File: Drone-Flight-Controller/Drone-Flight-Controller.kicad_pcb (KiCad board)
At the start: 4 copper layers, 56.5 x 59.8 mm, 36 parts, among them J1 Screw_Terminal_01x02, J2 Screw_Terminal_01x03, J3 Screw_Terminal_01x03, J4 Screw_Terminal_01x03, J5 Screw_Terminal_01x03, J6 Screw_Terminal_01x02, J7 Screw_Terminal_01x03, J8 Screw_Terminal_01x04, U1 LMR51430, U2 LF33_TO220, U3 ATmega328P-P, U4 MPU-6050, U5 BMP280, Y1 16mHz

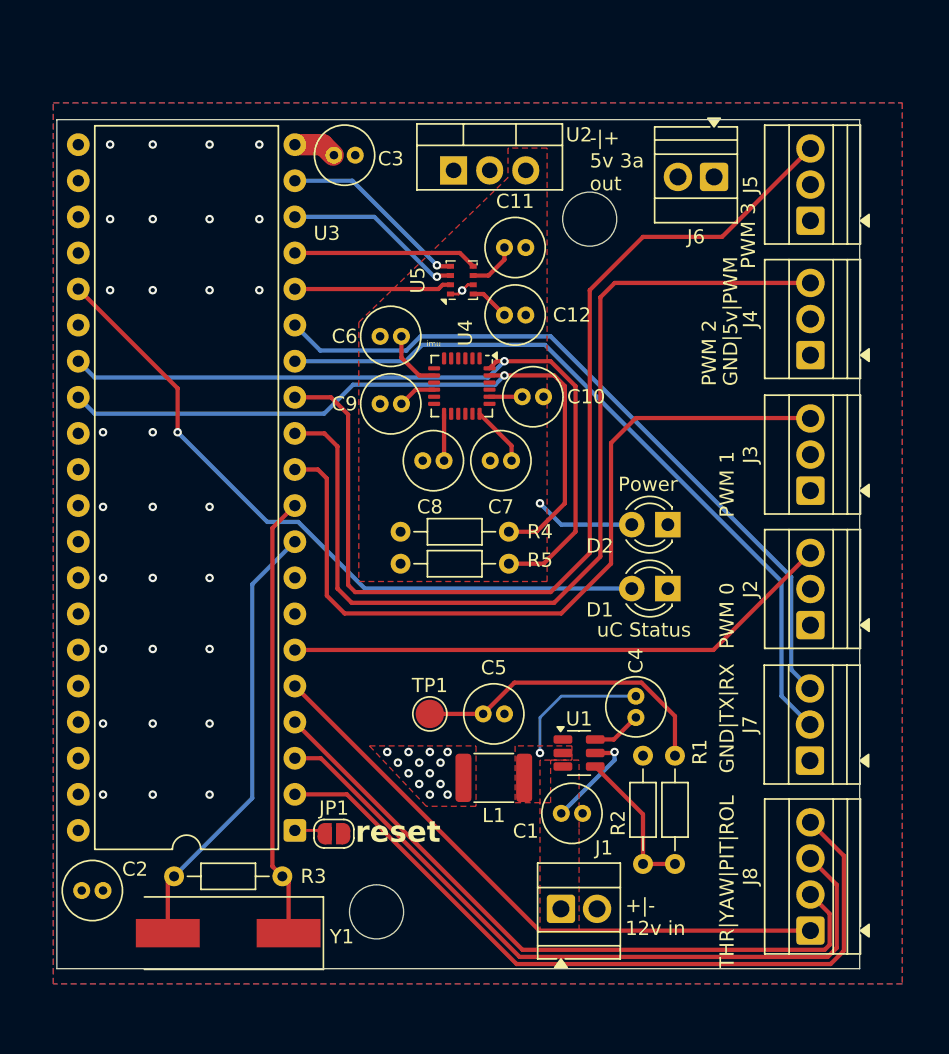
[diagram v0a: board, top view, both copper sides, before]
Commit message: move to stm32
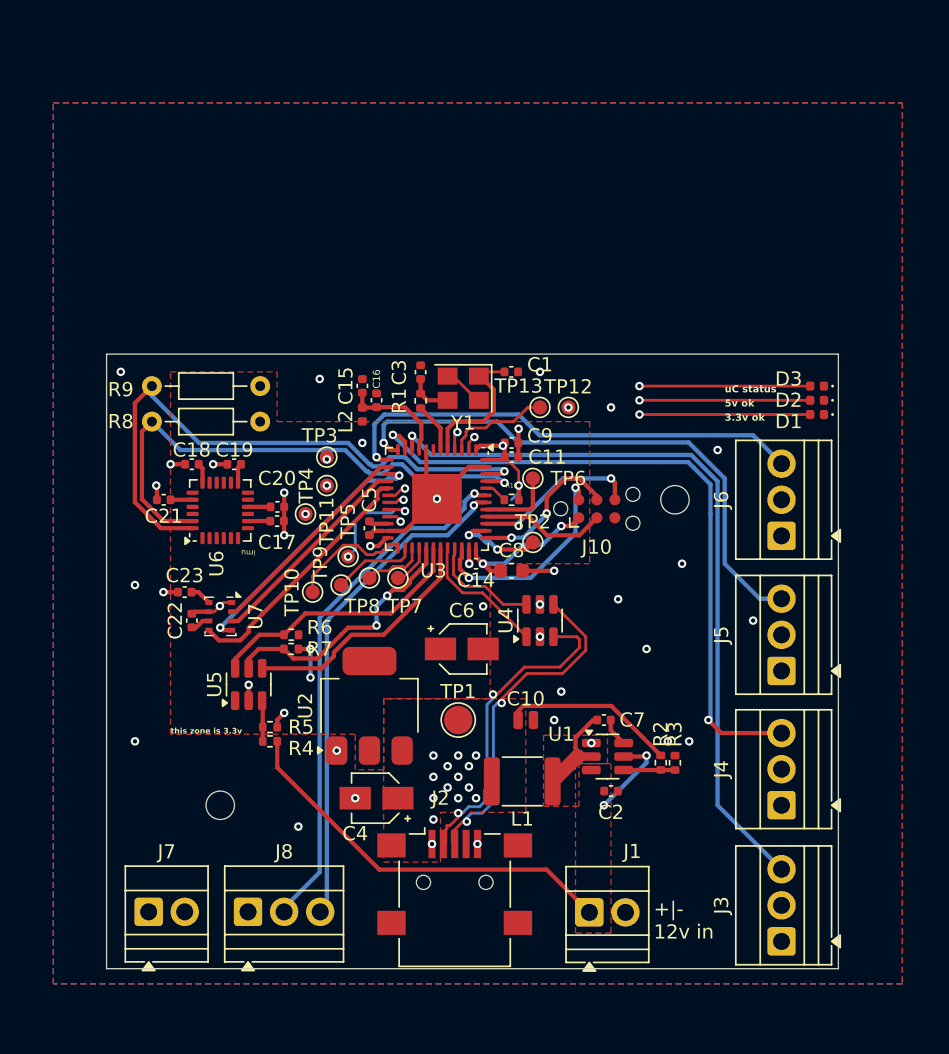
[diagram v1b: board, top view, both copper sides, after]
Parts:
- removed the C2 at (15.2, 68.5)
- removed JP1: SolderJumper_2_Open, Jumper:SolderJumper-2_P1.3mm_Open_RoundedPad1.0x1.5mm
- removed the R3 at (21.8, 67.5)
- added C1: 12p, Capacitor_SMD:C_0402_1005Metric, F.Cu at (45.5, 32.0)
- added C11: 100n, Capacitor_SMD:C_0402_1005Metric, F.Cu at (45.5, 38.0)
- added C14: 100n, Capacitor_SMD:C_0402_1005Metric, F.Cu at (43.0, 45.5)
- added C15: 1u, Capacitor_SMD:C_0402_1005Metric, F.Cu at (35.0, 33.0)
- added C16: 10n, Capacitor_SMD:C_0402_1005Metric, F.Cu at (36.0, 34.0)
- added C4: 10uF, Capacitor_SMD:CP_Elec_3x5.3, F.Cu at (36.0, 62.0)
- added C5: 2.2uF, Capacitor_SMD:C_0402_1005Metric, F.Cu at (35.5, 43.0)
- added C6: 10uF, Capacitor_SMD:CP_Elec_3x5.3, F.Cu at (42.0, 51.5)
- added C8: 4u7, Capacitor_SMD:C_0603_1608Metric, F.Cu at (45.5, 46.0)
- added C9: 100n, Capacitor_SMD:C_0402_1005Metric, F.Cu at (45.5, 37.0)
- added D3: LED, LED_SMD:LED_0402_1005Metric, F.Cu at (67.0, 33.0)
- added J10: Conn_ARM_SWD_TagConnect_TC2030-NL, Connector:Tag-Connect_TC2030-IDC-NL_2x03_P1.27mm_Vertical, F.Cu at (51.5, 41.6)
- added L2: 39n, Inductor_SMD:L_0402_1005Metric, F.Cu at (35.0, 35.0)
- added R1: 47, Resistor_SMD:R_0402_1005Metric, F.Cu at (39.1, 34.0)
- added R10: 10k, Resistor_SMD:R_0402_1005Metric, F.Cu at (45.5, 41.0)
- added R4: 1.5kOhm, Resistor_SMD:R_0402_1005Metric, F.Cu at (28.5, 58.0)
- added R5: 1kOhm, Resistor_SMD:R_0402_1005Metric, F.Cu at (28.5, 57.0)
- added R6: 10kOhm, Resistor_SMD:R_0402_1005Metric, F.Cu at (30.0, 50.5)
- added R7: 10kOhm, Resistor_SMD:R_0402_1005Metric, F.Cu at (30.0, 51.5)
- added TP10: TestPoint, TestPoint:TestPoint_Pad_D1.0mm, F.Cu at (31.5, 47.5)
- added TP11: TestPoint, TestPoint:TestPoint_Pad_D1.0mm, F.Cu at (31.0, 42.0)
- added TP12: TestPoint, TestPoint:TestPoint_Pad_D1.0mm, F.Cu at (49.5, 34.5)
- added TP13: TestPoint, TestPoint:TestPoint_Pad_D1.0mm, F.Cu at (47.5, 34.5)
- added TP2: TestPoint, TestPoint:TestPoint_Pad_D1.0mm, F.Cu at (47.0, 44.0)
- added TP3: TestPoint, TestPoint:TestPoint_Pad_D1.0mm, F.Cu at (32.5, 38.0)
- added TP4: TestPoint, TestPoint:TestPoint_Pad_D1.0mm, F.Cu at (32.5, 40.0)
- added TP5: TestPoint, TestPoint:TestPoint_Pad_D1.0mm, F.Cu at (34.0, 45.0)
- added TP6: TestPoint, TestPoint:TestPoint_Pad_D1.0mm, F.Cu at (47.0, 39.5)
- added TP7: TestPoint, TestPoint:TestPoint_Pad_D1.0mm, F.Cu at (37.5, 46.5)
- added TP8: TestPoint, TestPoint:TestPoint_Pad_D1.0mm, F.Cu at (35.5, 46.5)
- added TP9: TestPoint, TestPoint:TestPoint_Pad_D1.0mm, F.Cu at (33.5, 47.0)
- added U4: USBLC6-2SC6, Package_TO_SOT_SMD:SOT-23-6, F.Cu at (47.5, 49.5)
- added U5: ADC101C021CIMK, Package_TO_SOT_SMD:SOT-23-6, F.Cu at (27.0, 54.0)
- C10: renamed from C5; footprint Capacitor_THT:C_Radial_D4.0mm_H5.0mm_P1.50mm -> Capacitor_SMD:C_0504_1310Metric
- C17: renamed from C6; footprint Capacitor_THT:C_Radial_D4.0mm_H5.0mm_P1.50mm -> Capacitor_SMD:C_0402_1005Metric
- C18: renamed from C7; footprint Capacitor_THT:C_Radial_D4.0mm_H5.0mm_P1.50mm -> Capacitor_SMD:C_0402_1005Metric
- C19: renamed from C8; footprint Capacitor_THT:C_Radial_D4.0mm_H5.0mm_P1.50mm -> Capacitor_SMD:C_0402_1005Metric
- C2: renamed from C1; footprint Capacitor_THT:C_Radial_D4.0mm_H5.0mm_P1.50mm -> Capacitor_SMD:C_0402_1005Metric
- C20: renamed from C9; footprint Capacitor_THT:C_Radial_D4.0mm_H5.0mm_P1.50mm -> Capacitor_SMD:C_0402_1005Metric
- C21: renamed from C10; footprint Capacitor_THT:C_Radial_D4.0mm_H5.0mm_P1.50mm -> Capacitor_SMD:C_0402_1005Metric
- C22: renamed from C11; footprint Capacitor_THT:C_Radial_D4.0mm_H5.0mm_P1.50mm -> Capacitor_SMD:C_0402_1005Metric
- C23: renamed from C12; footprint Capacitor_THT:C_Radial_D4.0mm_H5.0mm_P1.50mm -> Capacitor_SMD:C_0402_1005Metric
- C3: value 100nF -> 12p; footprint Capacitor_THT:C_Radial_D4.0mm_H5.0mm_P1.50mm -> Capacitor_SMD:C_0402_1005Metric
- C7: renamed from C4; footprint Capacitor_THT:C_Radial_D4.0mm_H5.0mm_P1.50mm -> Capacitor_SMD:C_0402_1005Metric
- D1, D2: footprint LED_THT:LED_D3.0mm -> LED_SMD:LED_0402_1005Metric
- J2: value Screw_Terminal_01x03 -> USB_B_Micro; footprint TerminalBlock:TerminalBlock_Xinya_XY308-2.54-3P_1x03_P2.54mm_Horizontal -> Connector_USB:USB_Mini-B_Lumberg_2486_01_Horizontal
- J6: value Screw_Terminal_01x02 -> Screw_Terminal_01x03; footprint TerminalBlock:TerminalBlock_Xinya_XY308-2.54-2P_1x02_P2.54mm_Horizontal -> TerminalBlock:TerminalBlock_Xinya_XY308-2.54-3P_1x03_P2.54mm_Horizontal
- J7: value Screw_Terminal_01x03 -> Screw_Terminal_01x02; footprint TerminalBlock:TerminalBlock_Xinya_XY308-2.54-3P_1x03_P2.54mm_Horizontal -> TerminalBlock:TerminalBlock_Xinya_XY308-2.54-2P_1x02_P2.54mm_Horizontal
- J8: value Screw_Terminal_01x04 -> Screw_Terminal_01x03; footprint TerminalBlock:TerminalBlock_Xinya_XY308-2.54-4P_1x04_P2.54mm_Horizontal -> TerminalBlock:TerminalBlock_Xinya_XY308-2.54-3P_1x03_P2.54mm_Horizontal
- R2: renamed from R1; footprint Resistor_THT:R_Axial_DIN0204_L3.6mm_D1.6mm_P7.62mm_Horizontal -> Resistor_SMD:R_0402_1005Metric
- R3: renamed from R2; footprint Resistor_THT:R_Axial_DIN0204_L3.6mm_D1.6mm_P7.62mm_Horizontal -> Resistor_SMD:R_0402_1005Metric
- U2: value LF33_TO220 -> NCP1117-3.3_SOT223; footprint Package_TO_SOT_THT:TO-220-3_Vertical -> Package_TO_SOT_SMD:SOT-223-3_TabPin2
- U3: value ATmega328P-P -> STM32F401CBUx; footprint Package_DIP:DIP-40_W15.24mm -> Package_DFN_QFN:QFN-48-1EP_7x7mm_P0.5mm_EP3.5x3.5mm
- Y1: value 16mHz -> 16MHz; footprint Crystal:Crystal_SMD_HC49-SD -> Crystal:Crystal_SMD_3225-4Pin_3.2x2.5mm
- moved J7 47.7 mm to (20.0, 70.0), turned to 0 degrees
- moved Y1 41.8 mm to (42.1, 33.1)
- moved J8 39.6 mm to (27.0, 70.0), turned to 0 degrees
- moved U2 38.1 mm to (35.5, 55.5), turned to 90 degrees
- moved C22 34.2 mm to (23.0, 49.5), turned to 90 degrees
- moved J3 31.8 mm to (64.5, 72.1)
- moved J5 31.8 mm to (64.5, 53.0)
- moved J4 31.7 mm to (64.5, 62.5)
- moved C23 30.9 mm to (22.5, 47.5), turned to 0 degrees
- moved J2 30.9 mm to (41.5, 67.9), turned to 0 degrees
- moved U7 29.1 mm to (25.0, 49.2), turned to -90 degrees
- moved C21 26.3 mm to (21.0, 41.0), turned to 180 degrees
- moved J6 25.7 mm to (64.5, 43.5), turned to 90 degrees
- moved U3 25.4 mm to (40.2, 40.9), turned to -90 degrees
- moved C18 22.5 mm to (23.0, 38.5)
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- renumbered R4 to R8, R5 to R9, U4 to U6, U5 to U7
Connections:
- C3 pad 1: +5V -> Net-(C3-Pad1)
- D1 pad 2: Net-(D1-A) -> +3.3V
- D2 pad 2: +3.3V -> +5V
- J2 pad 1: GND -> +5V
- J2 pad 2: +5V -> USB_CONN_D-
- J2 pad 3: PWM_0 -> USB_CONN_D+
- J3 pad 3: PWM_1 -> PWM_0
- J4 pad 3: PWM_2 -> PWM_1
- J5 pad 3: PWM_3 -> PWM_2
- J6 pad 1: +5V -> GND
- J6 pad 2: GND -> +5V
- J7 pad 1: GND -> +5V
- J7 pad 2: UART_TX -> GND
- J8 pad 1: CONTROLLER_THROTTLE -> GND
- J8 pad 2: CONTROLLER_YAW -> UART_RX
- J8 pad 3: CONTROLLER_PITCH -> UART_TX
- U2 pad 1: +5V -> GND
- U2 pad 2: GND -> +3.3V
- U2 pad 3: +3.3V -> +5V
- U3 pad 1: Net-(JP1-A) -> +3.3V
- U3 pad 10: Net-(U3-XTAL2/PB7) -> PWM_0
- U3 pad 14: UART_TX -> BAROMETER_CSB
- U3 pad 15: UART_RX -> BAROMETER_SCK
- U3 pad 16: BAROMETER_CSB -> BAROMETER_SDI
- U3 pad 18: BAROMETER_SDI -> Net-(U3-PB0)
- U3 pad 19: BAROMETER_SCK -> Net-(U3-PB1)
- U3 pad 2: CONTROLLER_ROLL -> Net-(U3-PC13)
- U3 pad 20: +5V -> Net-(U3-PB2)
- U3 pad 22: GND -> Net-(U3-VCAP1)
- U3 pad 23: unconnected-(U3-PC0-Pad23) -> GND
- U3 pad 24: unconnected-(U3-PC1-Pad24) -> +3.3V
- U3 pad 25: Net-(D1-A) -> Net-(U3-PB12)
- U3 pad 26: unconnected-(U3-PC3-Pad26) -> Net-(U3-PB13)
- U3 pad 27: IMU_SDA -> Net-(U3-PB14)
- U3 pad 28: IMU_SCL -> Net-(U3-PB15)
- U3 pad 29: (no net) -> BATVOLTAGE_SCL
- U3 pad 3: CONTROLLER_PITCH -> Net-(U3-PC14)
- U3 pad 30: (no net) -> BATVOLTAGE_SDA
- U3 pad 31: (no net) -> BATVOLTAGE_ADDR
- U3 pad 32: (no net) -> USB_D-
- U3 pad 33: (no net) -> USB_D+
- U3 pad 34: (no net) -> SWDIO
- U3 pad 35: (no net) -> GND
- U3 pad 36: (no net) -> +3.3V
- U3 pad 37: (no net) -> SWCLK
- U3 pad 38: (no net) -> Net-(U3-PA15)
- U3 pad 39: (no net) -> SWO
- U3 pad 4: CONTROLLER_YAW -> LED_STATUS
- U3 pad 40: (no net) -> JTRST
- U3 pad 5: CONTROLLER_THROTTLE -> Net-(U3-PH0)
- U3 pad 6: PWM_0 -> Net-(U3-PH1)
- U3 pad 7: +5V -> NRST
- U3 pad 9: Net-(U3-XTAL1/PB6) -> +3.3VA
- U6 pad 9: unconnected-(U4-AD0-Pad9) -> IMU_ADDR
- Y1 pad 1: Net-(U3-XTAL2/PB7) -> Net-(U3-PH0)
- Y1 pad 2: Net-(U3-XTAL1/PB6) -> GND
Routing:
- net +3.3V: track 21.0 -> 80.5 mm, vias 1 -> 10
- net CONTROLLER_ROLL: track 54.0 -> 0.00 mm
- net CONTROLLER_PITCH: track 51.3 -> 0.00 mm
- net Net-(D1-A): track 49.5 -> 0.00 mm, vias 1 -> 0
- net CONTROLLER_YAW: track 48.5 -> 0.00 mm
- net CONTROLLER_THROTTLE: track 43.4 -> 0.00 mm
- net Net-(U3-PB10): track 53.5 -> 10.4 mm, vias 0 -> 2
- net PWM_3: track 72.8 -> 33.6 mm, vias 0 -> 1
- net GND: track 1.87 -> 34.4 mm, vias 30 -> 34
- net Net-(U3-XTAL1/PB6): track 31.3 -> 0.00 mm
- net Net-(U3-XTAL2/PB7): track 31.2 -> 0.00 mm
- net PWM_2: track 67.1 -> 39.2 mm, vias 0 -> 1
- net LED_STATUS: track 0.00 -> 27.5 mm, vias 0 -> 2
- net +12V: track 7.26 -> 34.4 mm, vias 1 -> 2
- net USB_CONN_D+: track 0.00 -> 24.0 mm, vias 0 -> 2
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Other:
- board size 56.5 x 59.8 mm -> 51.5 x 43.2 mm
- board text added: "3.3v ok"
- board text added: "5v ok"
- board text added: "this zone is 3.3v"
- board text added: "uC status"
- board text removed: "-|+ 5v 3a out"
- board text removed: "GND|5v|PWM"
- board text removed: "GND|TX|RX"
- board text removed: "PWM 0"
- board text removed: "PWM 1"
- board text removed: "PWM 2"
- board text removed: "PWM 3"
- board text removed: "Power"
- board text removed: "THR|YAW|PIT|ROL"
- board text removed: "reset"
- board text removed: "uC Status"

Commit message: move to more powerful mcu
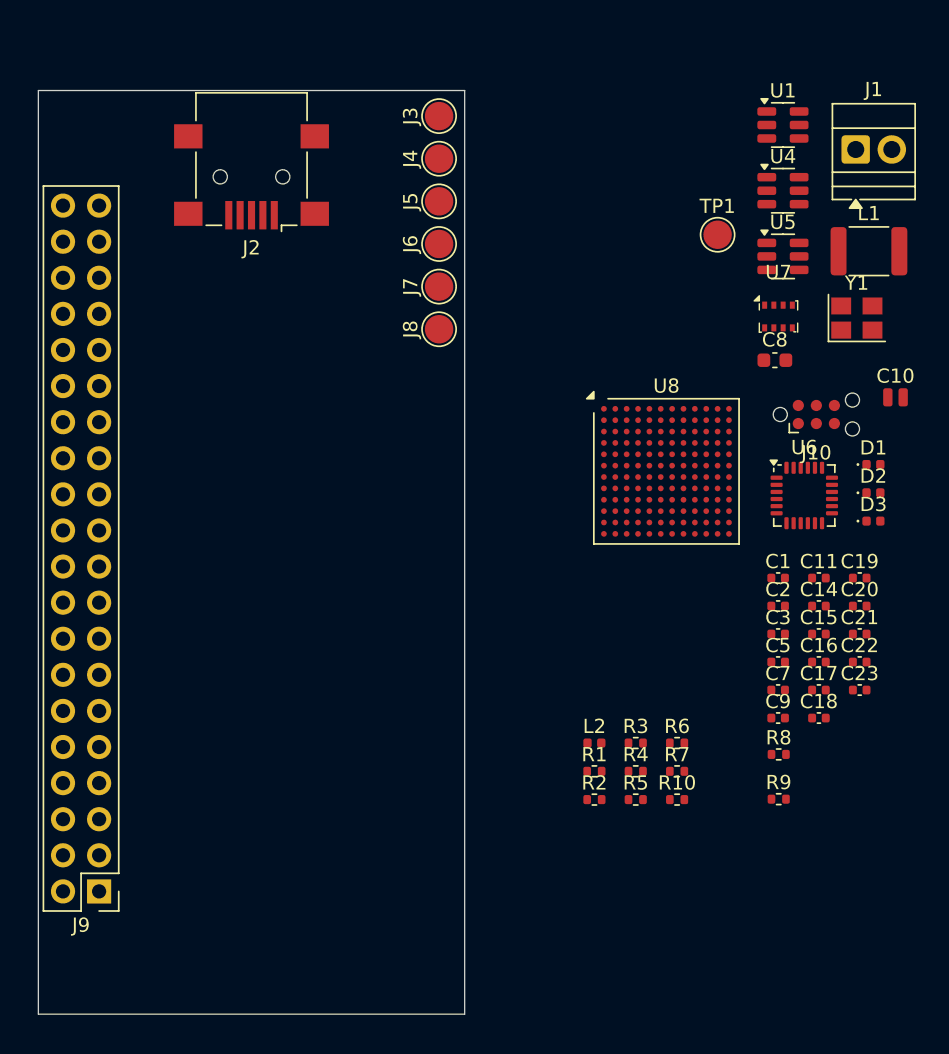
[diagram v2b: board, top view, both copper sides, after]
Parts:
- removed C4, C6: 10uF, Capacitor_SMD:CP_Elec_3x5.3
- removed TP10, TP11, TP12, TP13, TP2, TP3, TP4, TP5, TP6, TP7, TP8, TP9: TestPoint, TestPoint:TestPoint_Pad_D1.0mm
- removed U2: NCP1117-3.3_SOT223, Package_TO_SOT_SMD:SOT-223-3_TabPin2
- removed U3: STM32F401CBUx, Package_DFN_QFN:QFN-48-1EP_7x7mm_P0.5mm_EP3.5x3.5mm
- added J9: Raspberry_Pi_4, Connector_PinHeader_2.54mm:PinHeader_2x20_P2.54mm_Vertical, F.Cu at (16.5, 68.6)
- added U8: STM32F413ZHJx, Package_BGA:UFBGA-144_10x10mm_Layout12x12_P0.8mm, F.Cu at (56.4, 39.0)
- J3, J4, J5, J6, J8: value Screw_Terminal_01x03 -> TestPoint; footprint TerminalBlock:TerminalBlock_Xinya_XY308-2.54-3P_1x03_P2.54mm_Horizontal -> TestPoint:TestPoint_Pad_D2.0mm
- J7: value Screw_Terminal_01x02 -> TestPoint; footprint TerminalBlock:TerminalBlock_Xinya_XY308-2.54-2P_1x02_P2.54mm_Horizontal -> TestPoint:TestPoint_Pad_D2.0mm
- R8, R9: footprint Resistor_THT:R_Axial_DIN0204_L3.6mm_D1.6mm_P7.62mm_Horizontal -> Resistor_SMD:R_0402_1005Metric
- moved J3 62.9 mm to (40.4, 14.0)
- moved J1 56.9 mm to (69.7, 16.4)
- moved J2 51.7 mm to (27.2, 18.3), turned to 180 degrees
- moved J4 51.5 mm to (40.4, 17.0)
- moved C21 49.9 mm to (70.0, 50.5), turned to 0 degrees
- moved J7 48.5 mm to (40.4, 26.0), turned to 90 degrees
- moved U5 48.2 mm to (64.6, 23.9), turned to 0 degrees
- moved C23 48.0 mm to (70.0, 54.4)
- moved C18 47.6 mm to (67.1, 56.4), turned to 0 degrees
- moved C22 47.1 mm to (70.0, 52.4), turned to 0 degrees
- moved R9 46.7 mm to (64.3, 62.1), turned to 0 degrees
- moved U1 46.1 mm to (64.6, 14.6)
- moved C19 44.7 mm to (70.0, 46.5)
- moved U7 44.6 mm to (64.3, 28.1), turned to 0 degrees
- moved L1 44.6 mm to (70.7, 23.5), turned to 0 degrees
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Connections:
- C5 pad 2: Net-(U3-VCAP1) -> unconnected-(C5-Pad2)
- J3 pad 1: GND -> PWM_0
- J4 pad 1: GND -> PWM_1
- J5 pad 1: GND -> PWM_2
- J6 pad 1: GND -> PWM_3
- R1 pad 1: Net-(U3-PH1) -> unconnected-(R1-Pad1)
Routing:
- net +3.3V: track 80.5 -> 0.00 mm, vias 10 -> 0
- net PWM_0: track 53.0 -> 0.00 mm, vias 1 -> 0
- net PWM_1: track 47.6 -> 0.00 mm, vias 2 -> 0
- net IMU_SDA: track 43.1 -> 0.00 mm, vias 1 -> 0
- net PWM_2: track 39.2 -> 0.00 mm, vias 1 -> 0
- net IMU_SCL: track 38.5 -> 0.00 mm, vias 1 -> 0
- net UART_RX: track 37.2 -> 0.00 mm, vias 1 -> 0
- net UART_TX: track 35.2 -> 0.00 mm, vias 1 -> 0
- net +12V: track 34.4 -> 0.00 mm, vias 2 -> 0
- net GND: track 34.4 -> 0.00 mm, vias 34 -> 0
- net PWM_3: track 33.6 -> 0.00 mm, vias 1 -> 0
- net LED_STATUS: track 27.5 -> 0.00 mm, vias 2 -> 0
- net +5V: track 24.3 -> 0.00 mm, vias 16 -> 0
- net USB_CONN_D+: track 24.0 -> 0.00 mm, vias 2 -> 0
- net USB_CONN_D-: track 22.6 -> 0.00 mm, vias 2 -> 0
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- removed copper zone on F.Cu, net +12V
- removed copper zone on F.Cu, net +3.3V
- removed copper zone on F.Cu, net +5V
- removed copper zone on In1.Cu, net +5V
- removed copper zone on B.Cu, net GND
- removed copper zone on F.Cu, net GND
- removed copper zone on In2.Cu, net GND
- removed copper zone on F.Cu, net Net-(U1-SW)
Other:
- board size 51.5 x 43.2 mm -> 30 x 65 mm
- board text removed: "+|- 12v in"
- board text removed: "3.3v ok"
- board text removed: "5v ok"
- board text removed: "imu"
- board text removed: "this zone is 3.3v"
- board text removed: "uC status"
